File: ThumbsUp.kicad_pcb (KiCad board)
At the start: 2 copper layers, 250.9 x 280.9 mm, 172 parts, among them IC1 RP2040, IC2 W25Q128JVSIM, IC3 RP2040, IC4 W25Q128JVSIM, J1 Conn_01x04_Male, J10 Raiser_Male, J11 Raiser_Female, J12 Raiser_Male, J13 Raiser_Female, J14 Raiser_Male, J15 Raiser_Female, J16 Raiser_Male, J17 Raiser_Female, J18 Raiser_Male, J19 Raiser_Female, J2 Conn_01x04_Male, J20 Conn_01x04_Female, J21 Conn_01x04_Female, J22 Conn_01x04_Female, J23 Conn_01x04_Female, J24 Conn_01x04_Male, J25 Conn_01x04_Male, J26 Conn_01x04_Male, J27 Conn_01x04_Male, J28 Conn_01x04_Female, J29 Conn_01x04_Female, J3 Conn_01x04_Female, J30 Conn_01x04_Female, J31 Conn_01x04_Female, J32 USB_C_Receptacle_USB2.0, J33 Raiser_Male, J34 Raiser_Female, J35 Raiser_Male, J36 STX-3501-3N, J37 USB_C_Receptacle_USB2.0, J38 Raiser_Female, J39 Raiser_Male, J4 Conn_01x04_Male, J40 Raiser_Female, J41 Raiser_Male, J42 Raiser_Female, J43 Raiser_Male, J44 Raiser_Female, J45 Raiser_Male, J46 STX-3501-3N, J47 Raiser_Female, J48 Raiser_Male, J49 Raiser_Female, J5 Conn_01x04_Female, J50 Raiser_Male, J51 Raiser_Female, J52 Raiser_Male, J6 Conn_01x04_Male, J7 Conn_01x04_Male, J8 Conn_01x04_Male, J9 Raiser_Female, U1 NCP1117-3.3_SOT223, U2 NCP1117-3.3_SOT223, Y1 ABLS-12.000MHZ-B4-T, Y2 ABLS-12.000MHZ-B4-T

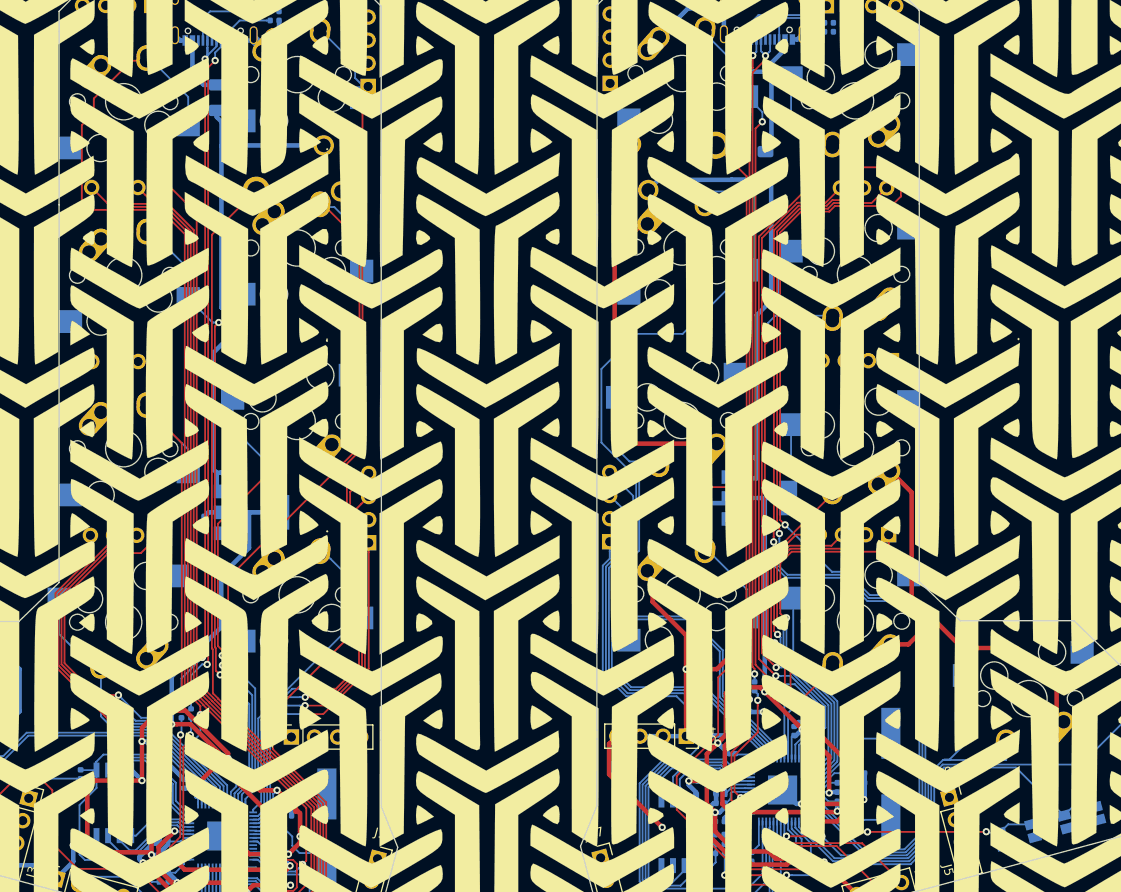
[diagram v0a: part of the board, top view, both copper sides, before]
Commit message: Moved the tracks out of L-inner corners
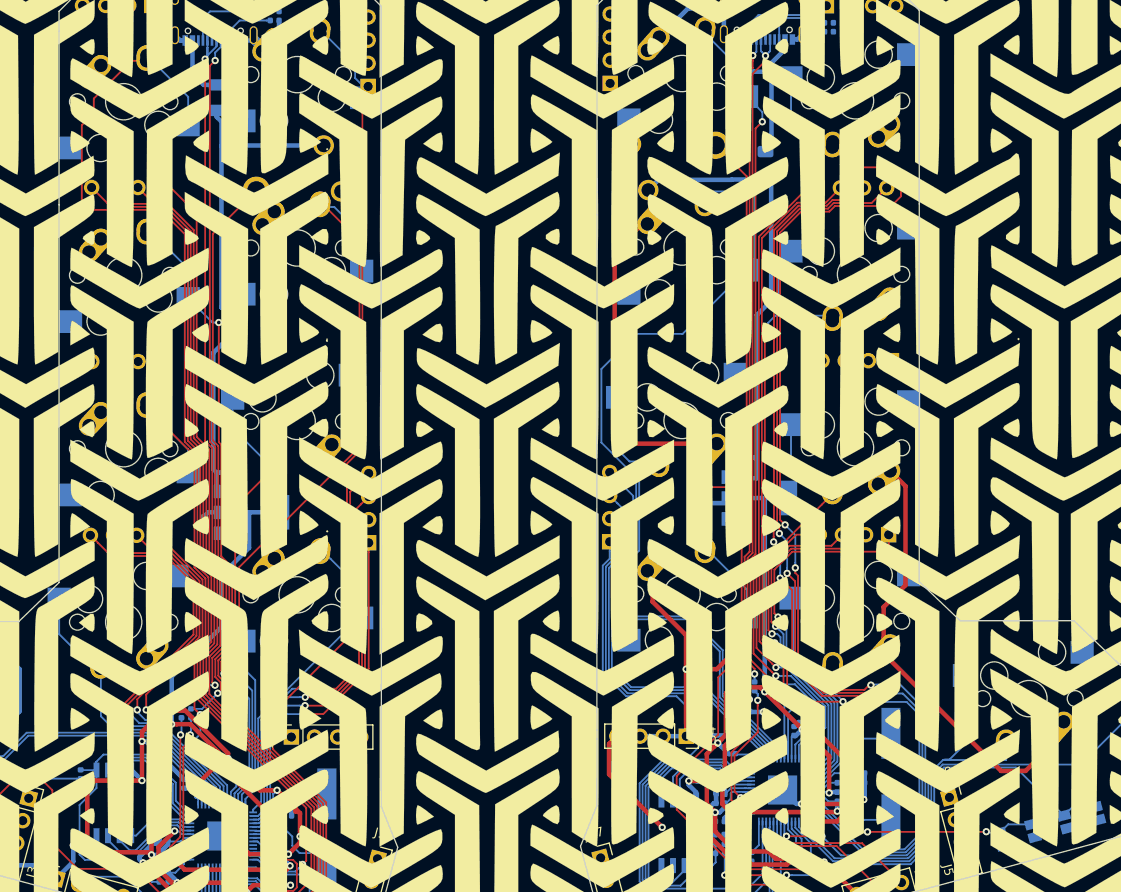
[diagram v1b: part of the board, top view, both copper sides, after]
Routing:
- net K_LCTL: track 45.8 -> 37.9 mm
- net L-BASE: track 422.3 -> 428.6 mm
- net K_C: track 40.9 -> 46.5 mm
- net K_M: track 23.9 -> 29.1 mm, vias 1 -> 2
- net K_Z: track 43.5 -> 40.6 mm
- net D-: track 77.5 -> 80.0 mm
- net D+: track 77.9 -> 80.3 mm
- net K_7: track 130.7 -> 133.1 mm, vias 3 -> 5
- net K_X: track 41.6 -> 43.5 mm
- net K_G: track 51.3 -> 49.9 mm
- net K_9: track 104.9 -> 103.9 mm, vias 1 -> 3
- net K_8: track 107.5 -> 106.5 mm, vias 1 -> 3
- net K_F: track 56.9 -> 57.9 mm
- net K_2: track 101.6 -> 102.6 mm
- net K_1: track 99.3 -> 100.3 mm
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
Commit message: Redrew the lower PCB
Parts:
- removed G*** (x3): LOGO, Silkscreens:Crowfeet75
- removed R17: 5.1K, Resistor_SMD:R_0402_1005Metric
- added J10: Raiser_Male, Connector_PinHeader_2.54mm:PinHeader_1x04_P2.54mm_Vertical, B.Cu at (91.0, 296.7)
- added J14: Raiser_Male, Connector_PinHeader_2.54mm:PinHeader_1x04_P2.54mm_Vertical, B.Cu at (129.7, 293.2)
- added J18: Raiser_Male, Connector_PinHeader_2.54mm:PinHeader_1x04_P2.54mm_Vertical, B.Cu at (117.1, 282.7)
- added J33: Raiser_Male, Connector_PinHeader_2.54mm:PinHeader_1x04_P2.54mm_Vertical, B.Cu at (192.8, 296.5)
- added J35: Raiser_Male, Connector_PinHeader_2.54mm:PinHeader_1x04_P2.54mm_Vertical, B.Cu at (166.6, 282.6)
- added J4: Conn_01x04_Male, Connector_PinHeader_2.54mm:PinHeader_1x04_P2.54mm_Vertical, B.Cu at (96.2, 304.4)
- added J48: Raiser_Male, Connector_PinHeader_2.54mm:PinHeader_1x04_P2.54mm_Vertical, B.Cu at (154.1, 293.1)
- added J6: Conn_01x04_Male, Connector_PinHeader_2.54mm:PinHeader_1x04_P2.54mm_Vertical, B.Cu at (187.8, 304.2)
- added MX18: SwLMOD, MX_Alps_Hybrid:MX-1U-NoLED_HotSwap, F.Cu at (119.1, 294.6)
- added MX22: SwLSHFT, MX_Alps_Hybrid:MX-1U-NoLED_HotSwap, F.Cu at (100.0, 294.6)
- added MX26: SwRSHFT, MX_Alps_Hybrid:MX-1U-NoLED_HotSwap, F.Cu at (183.9, 294.6)
- added MX30: SwRMOD, MX_Alps_Hybrid:MX-1U-NoLED_HotSwap, F.Cu at (164.8, 294.6)
- added MX57: SwLThumb, MX_Alps_Hybrid:MX-1U-NoLED_HotSwap, F.Cu at (101.6, 276.2)
- added MX58: SwRThumb, MX_Alps_Hybrid:MX-1U-NoLED_HotSwap, F.Cu at (178.0, 276.9)
- moved J15 0.12 mm to (108.9, 598.5)
- moved J20 0.12 mm to (54.1, 578.6)
- moved J21 0.12 mm to (103.7, 518.2)
- moved J22 0.12 mm to (103.7, 537.3)
- moved J23 0.12 mm to (103.5, 556.4)
- moved J44 0.12 mm to (126.5, 557.2)
- moved J49 0.12 mm to (102.7, 498.2)
- moved MX1 0.12 mm to (23.9, 524.8)
- moved MX11 0.12 mm to (81.1, 518.8)
- moved MX12 0.12 mm to (81.1, 537.9)
- moved MX13 0.12 mm to (81.1, 556.9)
- moved MX2 0.12 mm to (23.9, 543.9)
- moved MX3 0.12 mm to (23.9, 562.9)
- moved MX4 0.12 mm to (43.0, 528.8)
- moved MX45 0.12 mm to (23.9, 505.8)
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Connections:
- IC1 pad 29: Net-(IC1-Pad29) -> K_THUMBL
- IC3 pad 29: L-BASE -> K_THUMBR
- J3 pad 3: Net-(J3-Pad3) -> K_THUMBL
- J5 pad 1: Net-(J5-Pad1) -> K_THUMBR
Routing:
- net Net-(J30-Pad1): track 589.8 -> 0.00 mm
- net Net-(J22-Pad1): track 536.0 -> 0.00 mm
- net Net-(J6-Pad4): track 53.5 -> 107.0 mm
- net Net-(J4-Pad1): track 52.3 -> 104.5 mm
- net Net-(J6-Pad2): track 37.1 -> 74.2 mm
- net Net-(J4-Pad4): track 35.5 -> 71.1 mm
- net Net-(J4-Pad2): track 22.6 -> 45.2 mm
- net Net-(J6-Pad3): track 15.4 -> 30.7 mm
- net Net-(J15-Pad4): track 90.7 -> 105.8 mm
- net Net-(J23-Pad3): track 42.0 -> 56.8 mm
- net Net-(J44-Pad1): track 129.1 -> 143.6 mm
- net Net-(J29-Pad1): track 47.5 -> 61.5 mm
- net Net-(J44-Pad2): track 95.6 -> 109.1 mm
- net Net-(J44-Pad4): track 65.0 -> 76.7 mm
- net Net-(J44-Pad3): track 77.3 -> 87.4 mm
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- added copper zone on B.Cu, net Net-(J22-Pad1)
- added copper zone on B.Cu, net Net-(J30-Pad1)
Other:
- board size 250.9 x 280.9 mm -> 250.8 x 323.3 mm

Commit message: Reverted the schematics changres
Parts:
- removed the J10 at (91.0, 296.7)
- removed the J14 at (129.7, 293.2)
- removed the J18 at (117.1, 282.7)
- removed the J33 at (192.8, 296.5)
- removed the J35 at (166.6, 282.6)
- removed the J4 at (96.2, 304.4)
- removed the J48 at (154.1, 293.1)
- removed the J6 at (187.8, 304.2)
- removed the MX18 at (119.1, 294.6)
- removed the MX22 at (100.0, 294.6)
- removed the MX26 at (183.9, 294.6)
- removed the MX30 at (164.8, 294.6)
- removed MX57: SwLThumb, MX_Alps_Hybrid:MX-1U-NoLED_HotSwap
- removed MX58: SwRThumb, MX_Alps_Hybrid:MX-1U-NoLED_HotSwap
- added R17: 5.1K, Resistor_SMD:R_0402_1005Metric, B.Cu at (119.0, 467.4)
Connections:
- IC1 pad 29: K_THUMBL -> Net-(IC1-Pad29)
- IC3 pad 29: K_THUMBR -> L-BASE
- J3 pad 3: K_THUMBL -> Net-(J3-Pad3)
- J5 pad 1: K_THUMBR -> Net-(J5-Pad1)
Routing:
- net Net-(J6-Pad4): track 107.0 -> 53.5 mm
- net Net-(J4-Pad1): track 104.5 -> 52.3 mm
- net Net-(J6-Pad2): track 74.2 -> 37.1 mm
- net Net-(J4-Pad4): track 71.1 -> 35.5 mm
- net Net-(J4-Pad2): track 45.2 -> 22.6 mm
- net Net-(J6-Pad3): track 30.7 -> 15.4 mm
- net Net-(IC1-Pad29): track 0.00 -> 3.86 mm
- net K_THUMBL: track 3.86 -> 0.00 mm
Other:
- board size 250.8 x 323.3 mm -> 250.8 x 280.8 mm

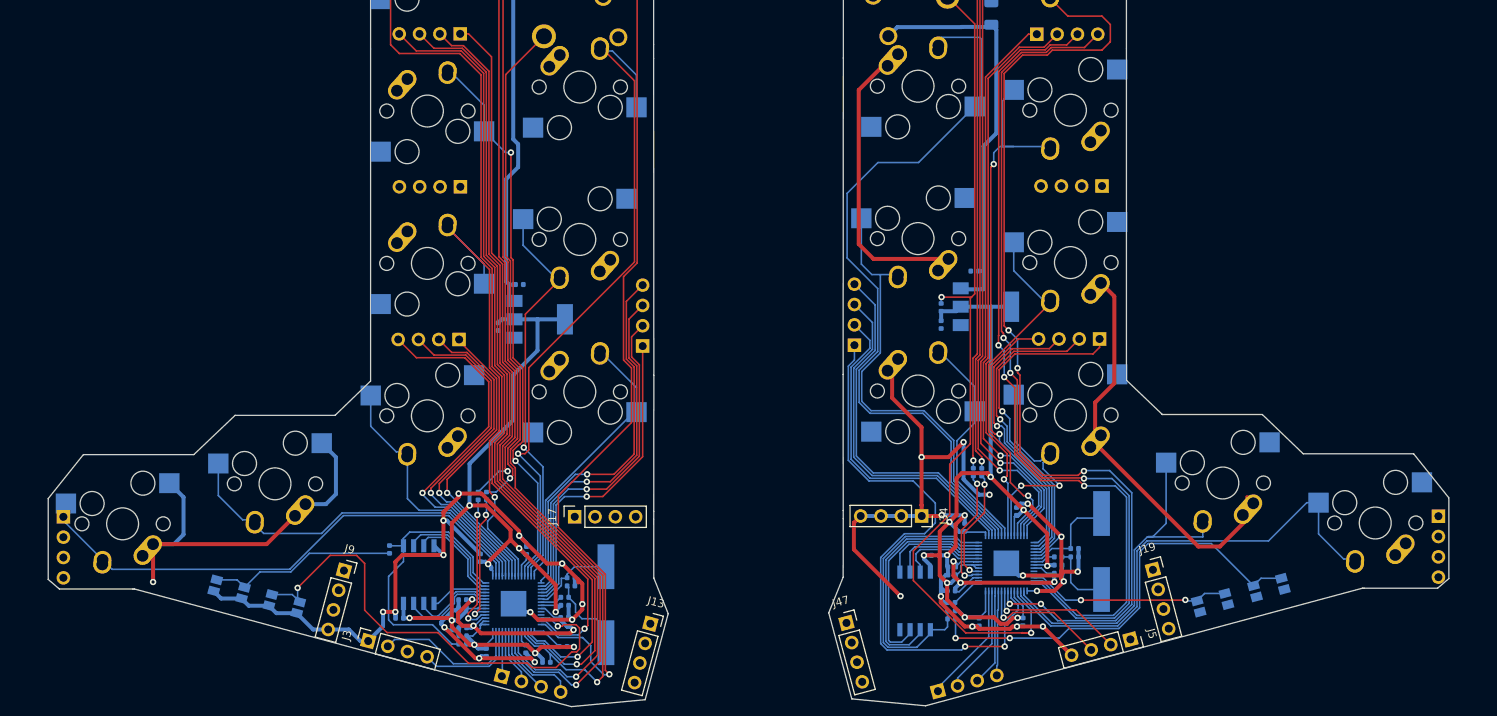
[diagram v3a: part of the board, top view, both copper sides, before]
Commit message: Adjusted outlines, replaced pushbuttons
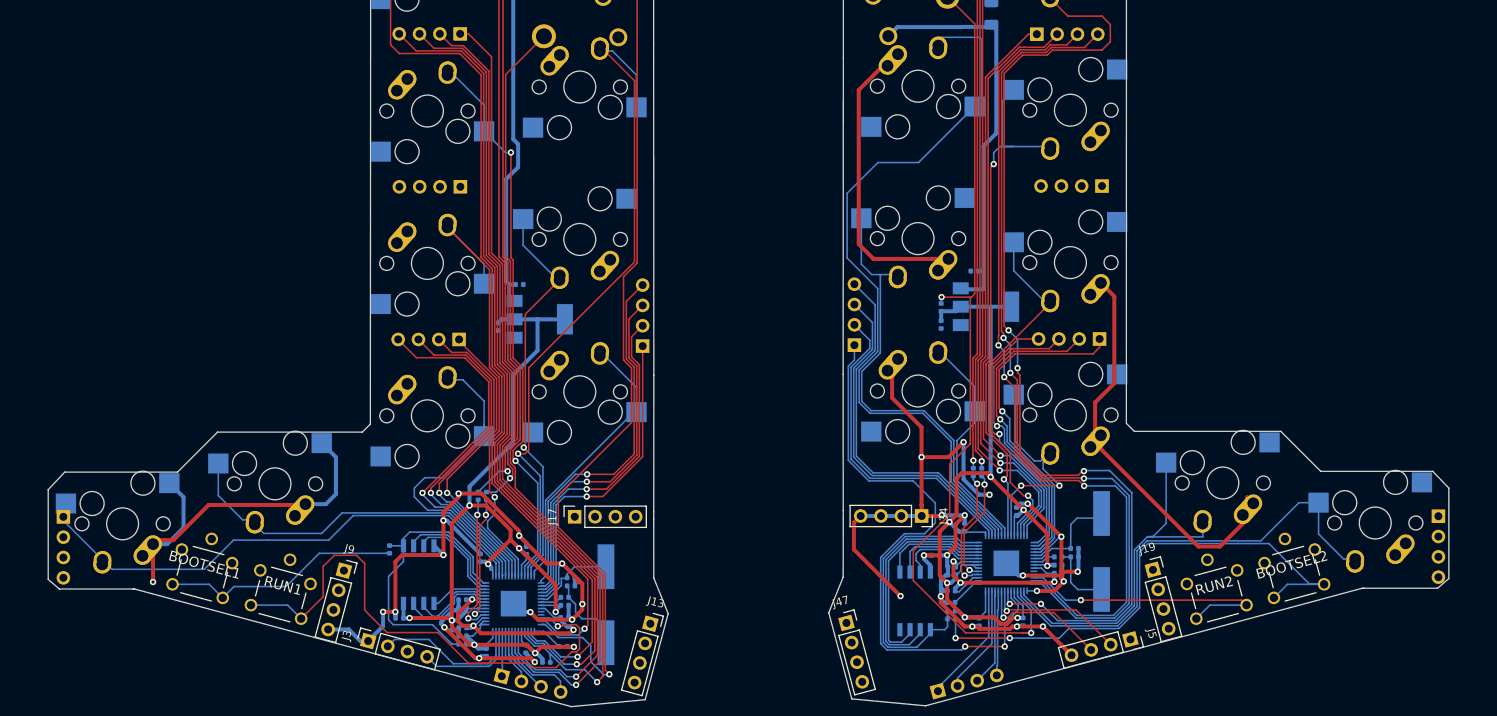
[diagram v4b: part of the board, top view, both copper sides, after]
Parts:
- BOOTSEL1, BOOTSEL2, RUN1, RUN2: value TL1016AAF220QG -> BUTT-4; footprint TL1016AAF220QG:TL1016AAF220QG -> KiCad:BUTT4; moved to F.Cu
- moved BOOTSEL1 3.87 mm to (73.9, 458.3), turned to 164.9 degrees
- moved BOOTSEL2 3.62 mm to (210.4, 458.3), turned to 195.1 degrees
- moved RUN1 1.25 mm to (83.7, 460.9), turned to 164.9 degrees
- moved RUN2 1.16 mm to (200.7, 460.9), turned to 195.1 degrees
- turned MX17 to 0 degrees
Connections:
- R12 pad 1: Net-(BOOTSEL2-Pad1) -> Net-(BOOTSEL2-PadA1)
- R3 pad 1: Net-(BOOTSEL1-Pad1) -> Net-(BOOTSEL1-PadA1)
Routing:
- net Net-(BOOTSEL2-PadA1): track 0.00 -> 66.6 mm, vias 0 -> 2
- net Net-(BOOTSEL2-Pad1): track 54.7 -> 0.00 mm, vias 2 -> 0
- net Net-(BOOTSEL1-PadA1): track 0.00 -> 30.1 mm
- net Net-(BOOTSEL1-Pad1): track 23.7 -> 0.00 mm
- net L-BASE: track 428.3 -> 411.5 mm
- net Net-(IC3-Pad26): track 25.5 -> 35.0 mm, vias 2 -> 1
- net K_V: track 33.1 -> 40.7 mm
- net Net-(IC1-Pad26): track 60.9 -> 65.6 mm, vias 2 -> 1
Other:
- outline, holes or cut-outs redrawn

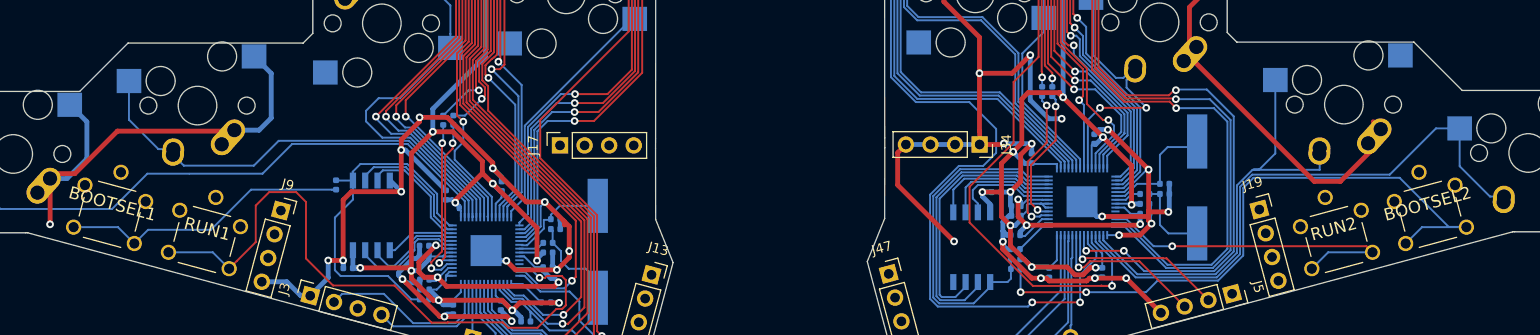
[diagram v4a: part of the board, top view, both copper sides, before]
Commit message: Moved buttons to back side, fixed disconnects
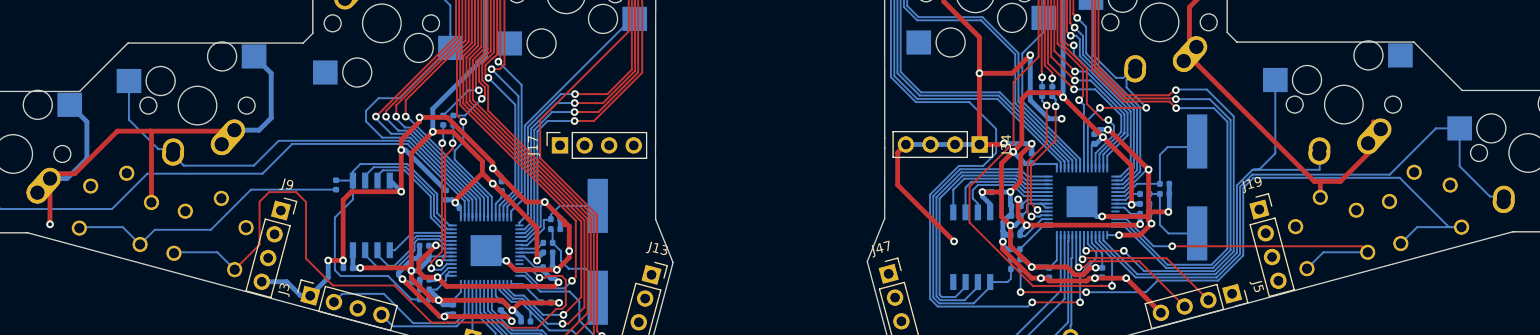
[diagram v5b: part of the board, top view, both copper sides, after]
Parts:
- BOOTSEL1, BOOTSEL2, RUN1, RUN2: moved to B.Cu
- moved BOOTSEL1 0.61 mm to (74.5, 458.4), turned to 344.9 degrees
- moved RUN1 0.58 mm to (84.3, 461.0), turned to 344.9 degrees
- moved BOOTSEL2 0.50 mm to (209.9, 458.3), turned to 15.1 degrees
- moved RUN2 0.50 mm to (200.2, 460.9), turned to 15.1 degrees
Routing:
- net L-BASE: track 411.5 -> 420.7 mm
- net K_V: track 40.7 -> 38.8 mm
- net Net-(IC3-Pad26): track 35.0 -> 34.5 mm
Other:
- board text added: "u/AK66666 ThumbsUp! v4 MX 2023-05-15"

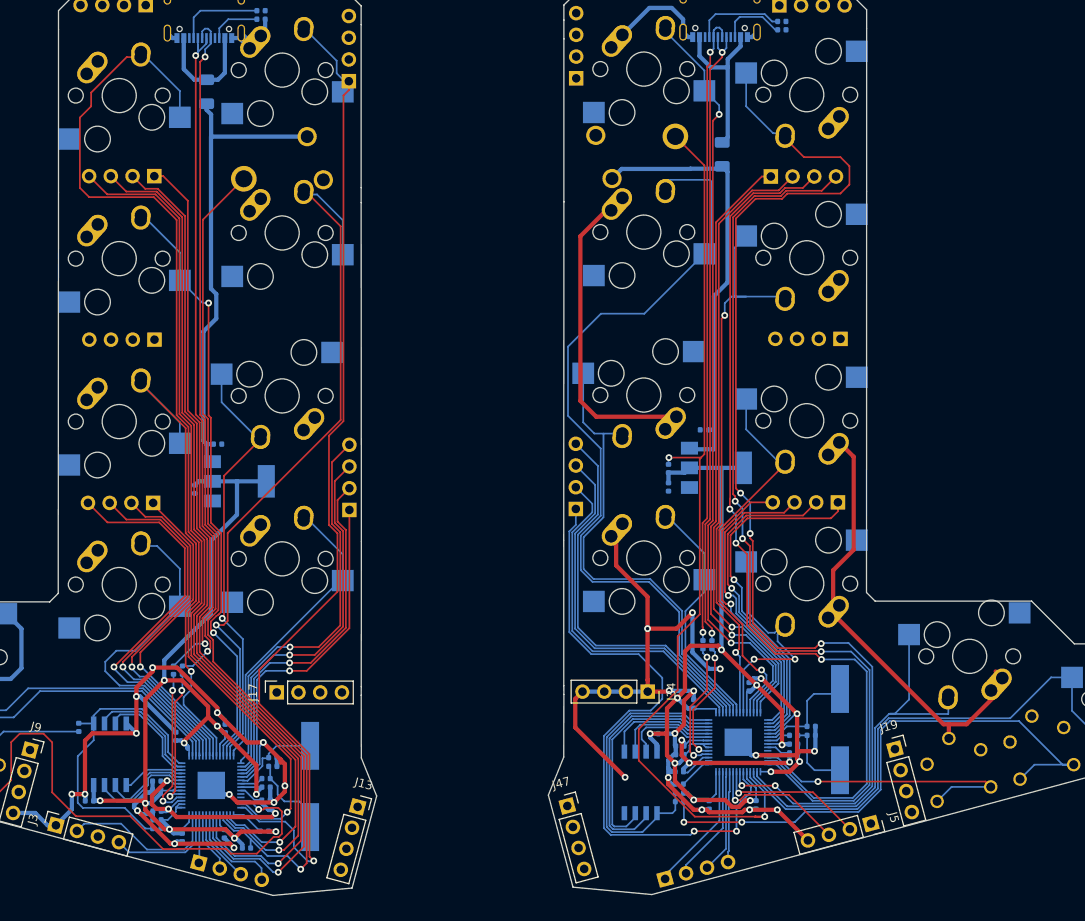
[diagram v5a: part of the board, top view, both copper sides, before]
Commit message: Moved tracks farther from the edges.
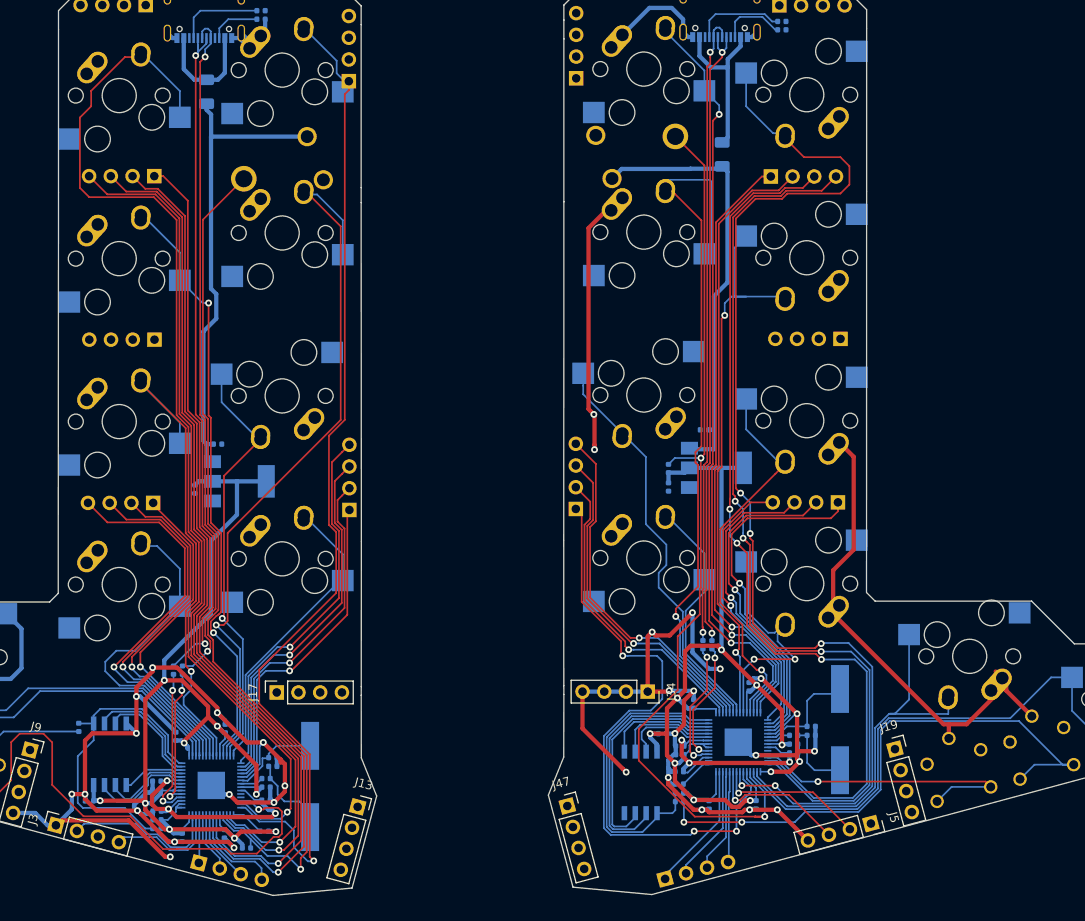
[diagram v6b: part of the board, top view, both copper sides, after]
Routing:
- net K_Y: track 92.6 -> 82.9 mm, vias 0 -> 1
- net L-BASE: track 420.7 -> 429.4 mm, vias 31 -> 34
- net K_H: track 55.6 -> 47.7 mm
- net K_O: track 42.7 -> 38.5 mm, vias 0 -> 1
- net K_I: track 45.4 -> 41.2 mm, vias 0 -> 1
- net K_P: track 40.1 -> 36.1 mm, vias 0 -> 1
- net K_E: track 46.1 -> 44.0 mm
- net K_W: track 44.3 -> 42.4 mm
- net K_Q: track 42.2 -> 40.6 mm
- net K_BSPC: track 73.7 -> 72.1 mm, vias 2 -> 3
- net K_ESC: track 39.2 -> 38.2 mm
- net K_RCTL: track 33.5 -> 32.8 mm
- net Net-(IC1-Pad26): track 65.8 -> 65.3 mm
